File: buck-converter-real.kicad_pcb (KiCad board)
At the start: 4 copper layers, 64 x 64 mm, 85 parts, among them J1 Conn_01x02_Pin, J1 USB_C_Receptacle_USB2.0_16P, J10 I2C1, J11 SWD, J12 Conn_01x04, J13 Conn_01x15, J2 SOL 24V, J3 Battery out (3V6-4V2) NiMH 3S, J5 Barrel_Jack_MountingPin, J6 DM3CS-SF, J8 I2C1, J9 SWD, Q1 CSD18540Q5B - 60-V, SW2 SW_Omron_B3FS, U1 AP2112K-3.3 (3V3 LDO), U2 CH32V203K8T6, U4 LMR51603XDBVR, U5 LM5109BMA (Mosfet Driver), Y1 8MHz 20pF

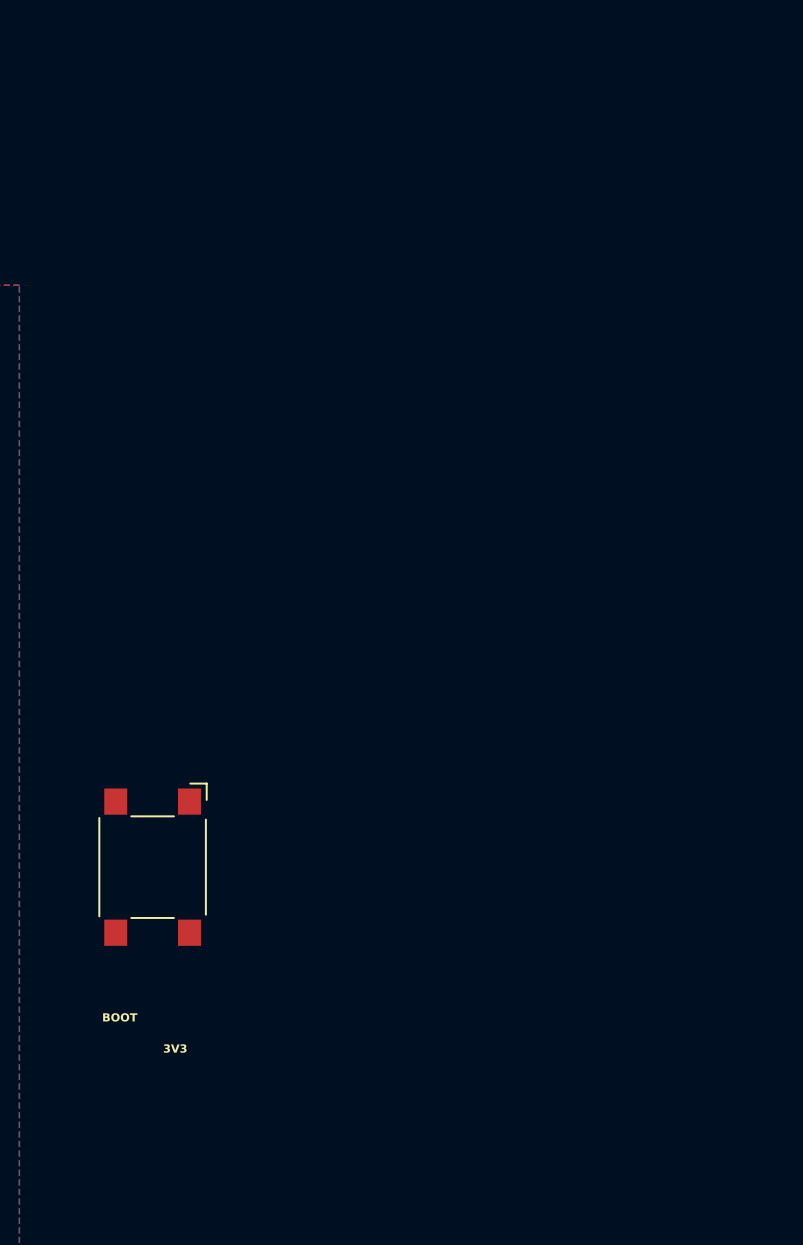
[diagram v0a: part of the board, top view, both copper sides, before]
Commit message: Add bucks/rs485/422
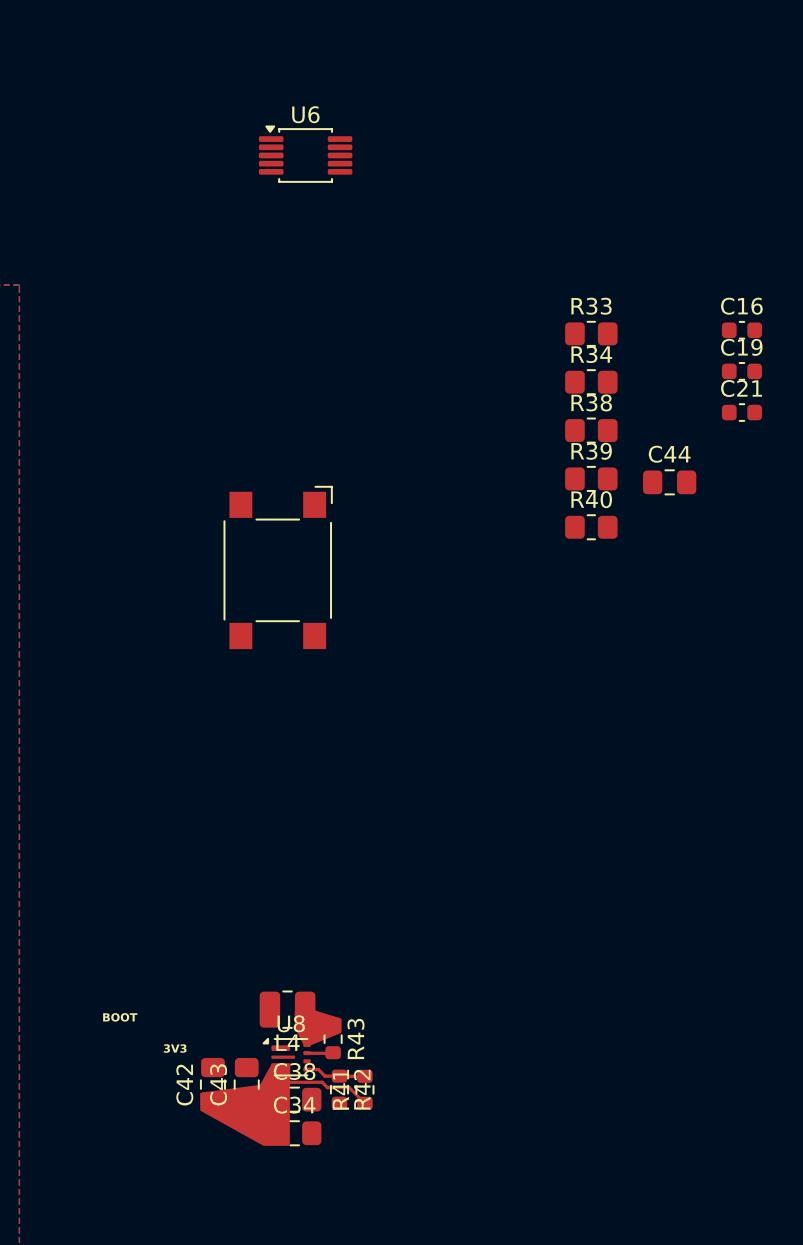
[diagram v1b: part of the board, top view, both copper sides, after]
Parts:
- added C16: 1n, Capacitor_SMD:C_0603_1608Metric, F.Cu at (178.2, 68.7)
- added C19: 1n, Capacitor_SMD:C_0603_1608Metric, F.Cu at (178.2, 71.2)
- added C21: 1n, Capacitor_SMD:C_0603_1608Metric, F.Cu at (178.2, 73.7)
- added C34: 100nF, Capacitor_SMD:C_0805_2012Metric_Pad1.18x1.45mm_HandSolder, F.Cu at (150.9, 117.7)
- added C38: 22uF 10V X7R/X5R 0805, Capacitor_SMD:C_0805_2012Metric_Pad1.18x1.45mm_HandSolder, F.Cu at (150.9, 115.6)
- added C42: 22uF 10V X7R/X5R 0805, Capacitor_SMD:C_0805_2012Metric_Pad1.18x1.45mm_HandSolder, F.Cu at (146.0, 114.7)
- added C43: 22uF 10V X7R/X5R 0805, Capacitor_SMD:C_0805_2012Metric_Pad1.18x1.45mm_HandSolder, F.Cu at (148.0, 114.7)
- added C44: 100nF 50V, Capacitor_SMD:C_0805_2012Metric_Pad1.18x1.45mm_HandSolder, F.Cu at (173.8, 78.0)
- added L4: 1uH lsat@5A 30mOhm AOTA-N252010S-1R0MT, Inductor_SMD:L_1008_2520Metric, F.Cu at (150.5, 110.1)
- added R33: 0, Resistor_SMD:R_0805_2012Metric_Pad1.20x1.40mm_HandSolder, F.Cu at (169.0, 68.9)
- added R34: 0, Resistor_SMD:R_0805_2012Metric_Pad1.20x1.40mm_HandSolder, F.Cu at (169.0, 71.8)
- added R38: 0, Resistor_SMD:R_0805_2012Metric_Pad1.20x1.40mm_HandSolder, F.Cu at (169.0, 74.8)
- added R39: 0, Resistor_SMD:R_0805_2012Metric_Pad1.20x1.40mm_HandSolder, F.Cu at (169.0, 77.7)
- added R40: 0, Resistor_SMD:R_0805_2012Metric_Pad1.20x1.40mm_HandSolder, F.Cu at (169.0, 80.7)
- added R41: 732k, Resistor_SMD:R_0603_1608Metric, F.Cu at (155.2, 115.0)
- added R42: 100k, Resistor_SMD:R_0603_1608Metric, F.Cu at (153.7, 115.0)
- added R43: 0, Resistor_SMD:R_0603_1608Metric, F.Cu at (153.3, 111.9)
- added U6: TPT482-VS2R, Package_SO:MSOP-10_3x3mm_P0.5mm, F.Cu at (151.6, 58.0)
- added U8: TPS61022, Package_DFN_QFN:Texas_RWU0007A_VQFN-7_2x2mm_P0.5mm, F.Cu at (150.7, 113.0)
- moved SW2 19.6 mm to (149.9, 83.3)
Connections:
- D2 pad 2: Net-(D2-A) -> unconnected-(D2-A-Pad2)
- D6 pad 2: +3.3V -> unconnected-(D6-A-Pad2)
- RST2 pad 2: Net-(D2-A) -> unconnected-(RST2-Pad2)
- U3 pad 20: Net-(D2-A) -> /Receiver Input Enable
- U3 pad 24: /VSENSE_VOUT -> Net-(U3-PB13)
- U3 pad 25: /RS_EN -> /Receiver Output Enable
- U3 pad 26: /VSENSE_VIN -> Net-(U3-PB14)
- U3 pad 27: /BAT_ISENSE -> Net-(U3-PA10)
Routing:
- net Net-(D2-A): track 53.5 -> 0.00 mm, vias 2 -> 0
- net (no net): track 0.00 -> 53.5 mm, vias 0 -> 2
- net +5V: track 0.00 -> 5.21 mm
- net unconnected-(D6-A-Pad2): track 0.00 -> 3.71 mm, vias 0 -> 1
- net +3.3V: track 50.6 -> 46.9 mm, vias 30 -> 29
- net Net-(U8-FB): track 0.00 -> 3.69 mm
- net Net-(U8-MODE): track 0.00 -> 1.61 mm

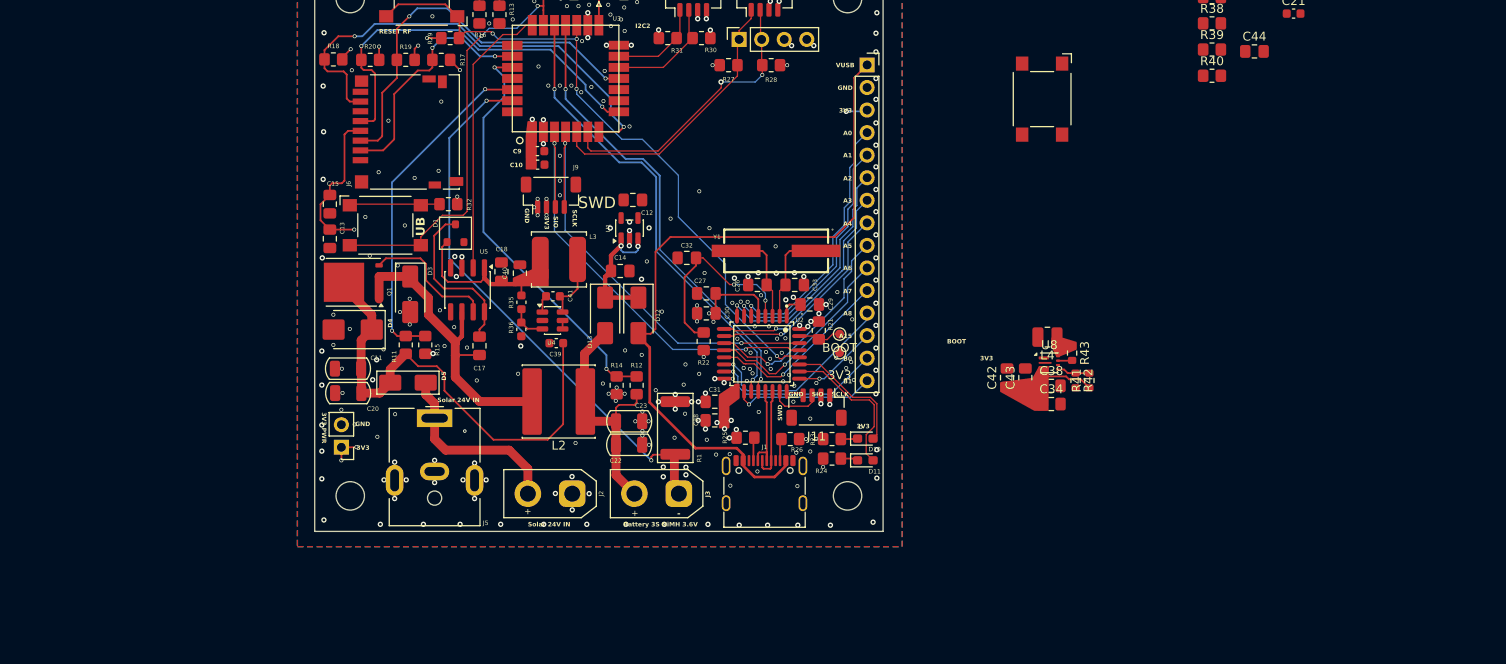
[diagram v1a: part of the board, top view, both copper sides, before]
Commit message: Buck layout, add headers.
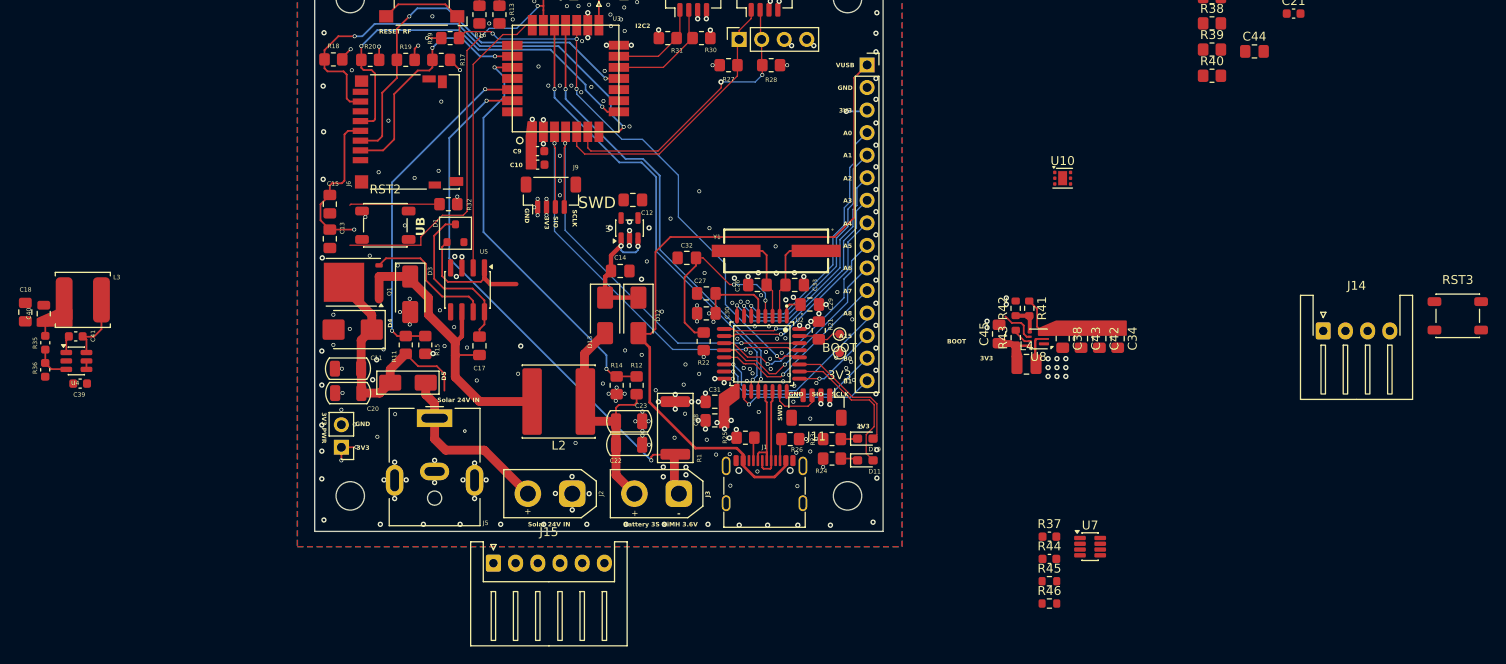
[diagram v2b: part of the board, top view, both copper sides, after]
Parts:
- removed SW2: SW_Omron_B3FS, Button_Switch_SMD:SW_SPST_Omron_B3FS-100xP
- added C45: 10uF 10V X7R/X5R 0805, Capacitor_SMD:C_0805_2012Metric_Pad1.18x1.45mm_HandSolder, F.Cu at (145.1, 109.8)
- added J14: Conn_01x04, Connector_JST:JST_XH_S4B-XH-A-1_1x04_P2.50mm_Horizontal, F.Cu at (181.6, 109.4)
- added J15: Conn_01x06, Connector_JST:JST_XH_S6B-XH-A_1x06_P2.50mm_Horizontal, F.Cu at (88.1, 135.6)
- added R37: 120, Capacitor_SMD:C_0603_1608Metric, F.Cu at (150.7, 132.6)
- added R44: 120, Capacitor_SMD:C_0603_1608Metric, F.Cu at (150.7, 135.1)
- added R45: 0, Resistor_SMD:R_0603_1608Metric, F.Cu at (150.7, 137.6)
- added R46: 0, Resistor_SMD:R_0603_1608Metric, F.Cu at (150.7, 140.1)
- added RST3: SW_Omron_B3FS, Button_Switch_SMD:SW_SPST_PTS647_Sx38, F.Cu at (196.7, 107.7)
- added U10: TLV75733PDRV, Package_SON:WSON-6-1EP_2x2mm_P0.65mm_EP1x1.6mm, F.Cu at (152.2, 92.2)
- added U7: TCAN3414DDFR, Package_TO_SOT_SMD:TSOT-23-8, F.Cu at (155.3, 133.7)
- RST2: footprint Button_Switch_SMD:SW_SPST_Omron_B3FS-100xP -> Button_Switch_SMD:SW_SPST_PTS647_Sx38
- moved C41 53.9 mm to (41.1, 110.0)
- moved C18 53.8 mm to (35.4, 107.3)
- moved R35 53.8 mm to (37.7, 110.8)
- moved U4 53.8 mm to (41.2, 112.8)
- moved C39 53.8 mm to (41.6, 115.4)
- moved L3 53.8 mm to (41.9, 105.9)
- moved R36 53.8 mm to (37.6, 113.8)
- moved C40 53.8 mm to (37.5, 107.5)
- moved C42 11.3 mm to (156.4, 110.3), turned to -90 degrees
- moved R41 10.6 mm to (148.5, 106.9), turned to -90 degrees
- moved R42 10.6 mm to (146.9, 106.9), turned to 90 degrees
- moved C34 10.5 mm to (158.4, 110.3), turned to -90 degrees
- moved C43 7.67 mm to (154.3, 110.3), turned to -90 degrees
- moved R43 6.58 mm to (146.9, 110.2), turned to 90 degrees
- moved C38 5.48 mm to (152.2, 110.3), turned to -90 degrees
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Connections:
- U1 pad 1: Net-(D12-K) -> unconnected-(U1-VIN-Pad1)
- U1 pad 2: GND -> unconnected-(U1-GND-Pad2)
- U1 pad 3: Net-(D12-K) -> unconnected-(U1-EN-Pad3)
- U1 pad 5: +3.3V -> unconnected-(U1-VOUT-Pad5)
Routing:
- net /Solar In: track 55.7 -> 30.1 mm
- net /5V EN: track 0.00 -> 4.24 mm
- net Net-(U8-FB): track 3.69 -> 0.00 mm
- net /Solar +: track 21.5 -> 19.8 mm
- net +5V: track 5.21 -> 3.65 mm
- net Net-(U8-MODE): track 1.61 -> 2.35 mm
- net (no net): vias 2 -> 15

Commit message: Change buck IC
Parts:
- removed C40: 15uF, Capacitor_SMD:C_0805_2012Metric
- added C46: 22uF 10V X7R/X5R 0805, Capacitor_SMD:C_0805_2012Metric_Pad1.18x1.45mm_HandSolder, F.Cu at (52.7, 110.8)
- added C47: 22uF 10V X7R/X5R 0805, Capacitor_SMD:C_0805_2012Metric_Pad1.18x1.45mm_HandSolder, F.Cu at (52.7, 113.8)
- added C48: 100nF, Capacitor_SMD:C_0603_1608Metric, F.Cu at (48.3, 110.6)
- added R47: 1.5m, Capacitor_SMD:C_0603_1608Metric, F.Cu at (48.3, 113.1)
- added R48: 100k, Capacitor_SMD:C_0603_1608Metric, F.Cu at (48.3, 115.6)
- L3: value 56 uH -> 68u; footprint Inductor_SMD:L_TDK_VLS6045EX_VLS6045AF -> Inductor_SMD:L_Chilisin_BWVS00606020
- R35: value 309 -> 309k
- R36: value 22.1 -> 22.1k
- U4: value LMR51603XDBVR -> LMR51610YDBVR
- U5: value LM5109BMA (Mosfet Driver) -> LM5109BMA/NOPB
- moved R35 4.41 mm to (38.0, 115.2), turned to 0 degrees
- moved R36 2.91 mm to (38.0, 116.7), turned to 180 degrees
- moved L3 2.25 mm to (39.6, 106.1)
- moved C39 0.44 mm to (41.1, 115.3)
- moved C18 0.25 mm to (35.2, 107.2)
- moved C41 0.17 mm to (41.1, 110.2)
- moved U4 0.08 mm to (41.1, 112.7)
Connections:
- U4 pad 4: /Solar In -> Net-(U4-EN)
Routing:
- net Net-(U4-SW): track 7.58 -> 0.00 mm
- net Net-(U4-FB): track 4.18 -> 0.00 mm
- net Net-(U4-CB): track 1.95 -> 0.00 mm
- net /12V-buck: track 15.8 -> 14.3 mm

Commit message: Remapping board
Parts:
- removed J2: SOL 24V, Connector_AMASS:AMASS_XT30UPB-F_1x02_P5.0mm_Vertical
- removed J3: Battery out (3V6-4V2) NiMH 3S, Connector_AMASS:AMASS_XT30UPB-F_1x02_P5.0mm_Vertical
- removed J5: Barrel_Jack_MountingPin, Connector_BarrelJack:BarrelJack_CUI_PJ-063AH_Horizontal
- moved U10 137.6 mm to (20.8, 132.9), turned to -90 degrees
- moved C12 86.4 mm to (23.9, 127.6)
- moved C14 86.4 mm to (22.5, 135.6)
- moved D12 86.4 mm to (24.6, 140.6)
- moved D13 86.4 mm to (20.8, 140.6)
- moved J14 81.1 mm to (116.3, 157.7)
- moved C11 73.5 mm to (131.6, 156.2)
- moved C20 73.5 mm to (131.7, 159.0)
- moved D4 73.5 mm to (132.2, 151.8)
- moved R11 73.5 mm to (138.1, 153.5)
- moved R15 73.5 mm to (140.3, 153.5)
- moved D3 60.8 mm to (45.1, 155.9)
- moved D1 59.3 mm to (57.8, 151.8), turned to 0 degrees
- moved L2 59.0 mm to (51.5, 156.6)
- moved C22 57.2 mm to (58.3, 157.4)
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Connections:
- net Net-(D12-K) renamed /BATT-IN
- J14 pad 1: unconnected-(J14-Pin_1-Pad1) -> GND
- J14 pad 2: unconnected-(J14-Pin_2-Pad2) -> GND
- J14 pad 3: unconnected-(J14-Pin_3-Pad3) -> /Solar +
- J14 pad 4: unconnected-(J14-Pin_4-Pad4) -> /Solar +
- J15 pad 1: unconnected-(J15-Pin_1-Pad1) -> +BATT
- J15 pad 2: unconnected-(J15-Pin_2-Pad2) -> +BATT
- J15 pad 3: unconnected-(J15-Pin_3-Pad3) -> +BATT
- J15 pad 4: unconnected-(J15-Pin_4-Pad4) -> /BAT_ISENSE
- J15 pad 5: unconnected-(J15-Pin_5-Pad5) -> /BAT_ISENSE
- J15 pad 6: unconnected-(J15-Pin_6-Pad6) -> /BAT_ISENSE
- U10 pad 2: unconnected-(U10-NC-Pad2) -> GND
- U10 pad 5: unconnected-(U10-NC-Pad5) -> GND
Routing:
- net /BAT_ISENSE: track 61.8 -> 0.00 mm, vias 2 -> 0
- net /VSENSE_VOUT: track 46.9 -> 0.00 mm, vias 2 -> 0
- net /VSENSE_VIN: track 38.6 -> 0.00 mm, vias 2 -> 0
- net Net-(D3-K): track 36.2 -> 0.00 mm
- net /I2C-1-SDA: track 33.0 -> 0.00 mm
- net /I2C-1-SCL: track 31.8 -> 0.00 mm
- net /Solar In: track 30.1 -> 3.83 mm
- net +BATT: track 23.7 -> 0.00 mm
- net /PWM_HI: track 32.1 -> 9.13 mm
- net Net-(U3-PA10): track 0.00 -> 22.4 mm, vias 0 -> 1
- net /Solar +: track 19.8 -> 0.00 mm
- net Net-(U3-PB14): track 0.00 -> 17.9 mm, vias 0 -> 2
- net /BATT-IN: track 15.2 -> 0.00 mm, vias 2 -> 0
- net /I2C-2-SCA: track 13.0 -> 0.00 mm
- net Net-(Q1-G): track 15.2 -> 3.88 mm
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
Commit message: Remapping board, placing groups
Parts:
- moved C48 67.7 mm to (102.1, 98.2), turned to -90 degrees
- moved C47 66.5 mm to (100.2, 97.8), turned to 90 degrees
- moved C46 64.8 mm to (98.2, 97.8), turned to 90 degrees
- moved C13 62.8 mm to (86.8, 38.7), turned to 180 degrees
- moved L3 60.3 mm to (99.9, 103.2), turned to -90 degrees
- moved C15 60.3 mm to (90.7, 38.7), turned to 180 degrees
- moved C20 59.2 mm to (94.8, 112.7)
- moved C11 58.9 mm to (94.8, 110.2)
- moved U5 58.3 mm to (80.8, 95.8)
- moved C18 58.3 mm to (85.6, 96.3)
- moved C22 58.3 mm to (85.4, 105.8)
- moved C23 58.3 mm to (85.4, 103.2)
- moved D1 58.3 mm to (84.8, 100.2)
- moved D3 58.3 mm to (72.2, 104.3)
- moved L2 58.3 mm to (78.5, 105.0)
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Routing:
- net VBUS: track 81.5 -> 6.96 mm
- net /SPI-CITO: track 53.0 -> 0.00 mm, vias 2 -> 0
- net /SPI-SCK: track 45.1 -> 0.00 mm, vias 2 -> 0
- net /SPI-COTI: track 44.7 -> 0.00 mm, vias 2 -> 0
- net (no net): track 44.6 -> 0.00 mm, vias 39 -> 13
- net +3.3V: track 48.1 -> 20.0 mm, vias 32 -> 14
- net /SPI-CS: track 28.0 -> 0.00 mm, vias 2 -> 0
- net Net-(U3-PA10): track 22.4 -> 0.00 mm, vias 1 -> 0
- net Net-(U3-PB14): track 17.9 -> 0.00 mm, vias 2 -> 0
- net /PWM_HI: track 9.13 -> 0.65 mm
- net /12V-buck: track 11.0 -> 19.0 mm
- net Net-(D3-K): track 0.00 -> 7.33 mm
- net /SWD-WIO-IO: track 51.7 -> 45.1 mm
- net /SWD-WIO-CLK: track 50.0 -> 43.3 mm
- net +BATT: track 0.00 -> 4.20 mm
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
